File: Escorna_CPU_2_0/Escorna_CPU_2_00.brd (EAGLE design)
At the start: 50.2 x 85 mm, 59 parts, among them IC1 ULN2803, U2 ESP01, X1 AK550/2

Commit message: Act. bottom layer
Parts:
- Z1: value F/CM12P -> CFG12
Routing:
- net RAW: track 141.1 -> 181.6 mm
- net D10: track 33.0 -> 30.6 mm
- net S3: track 31.4 -> 30.8 mm
- net TX: track 22.6 -> 22.0 mm
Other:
- board text added: "1538"

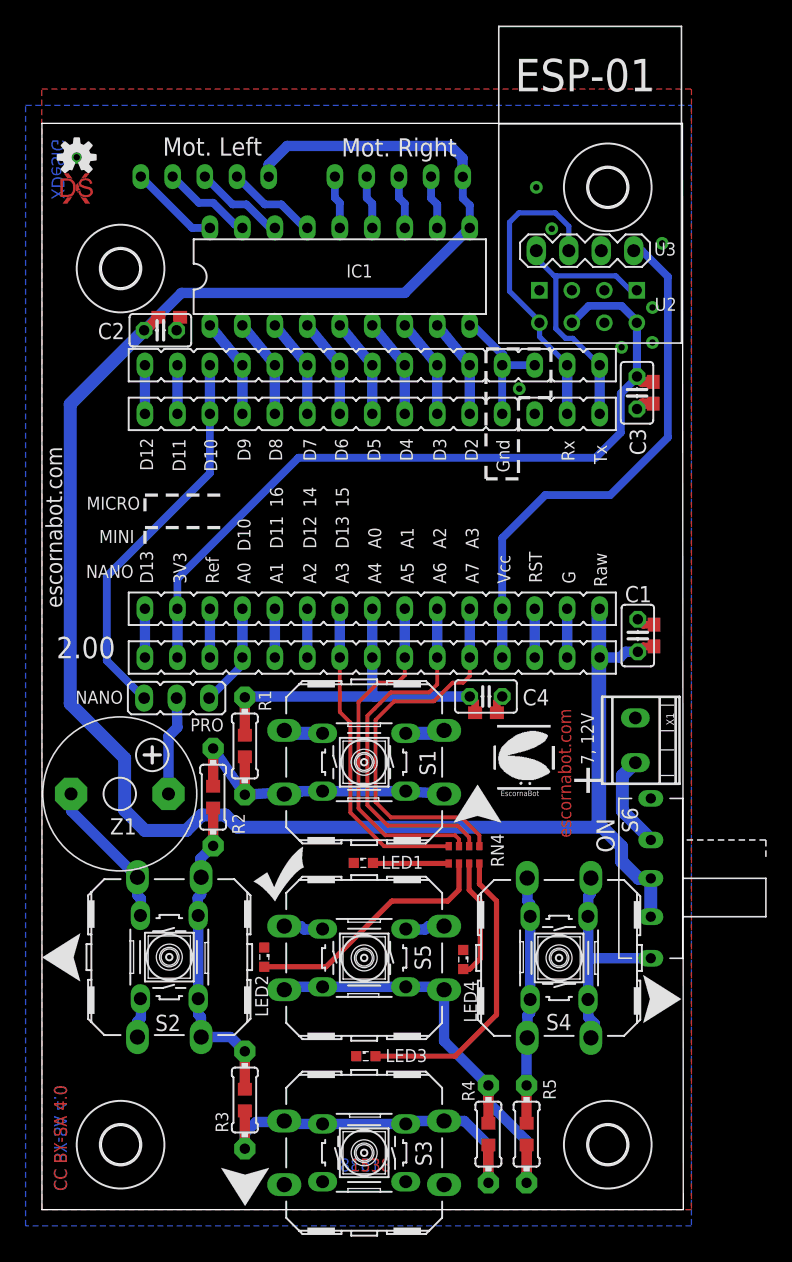
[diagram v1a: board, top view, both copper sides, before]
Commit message: Act. slikscreen
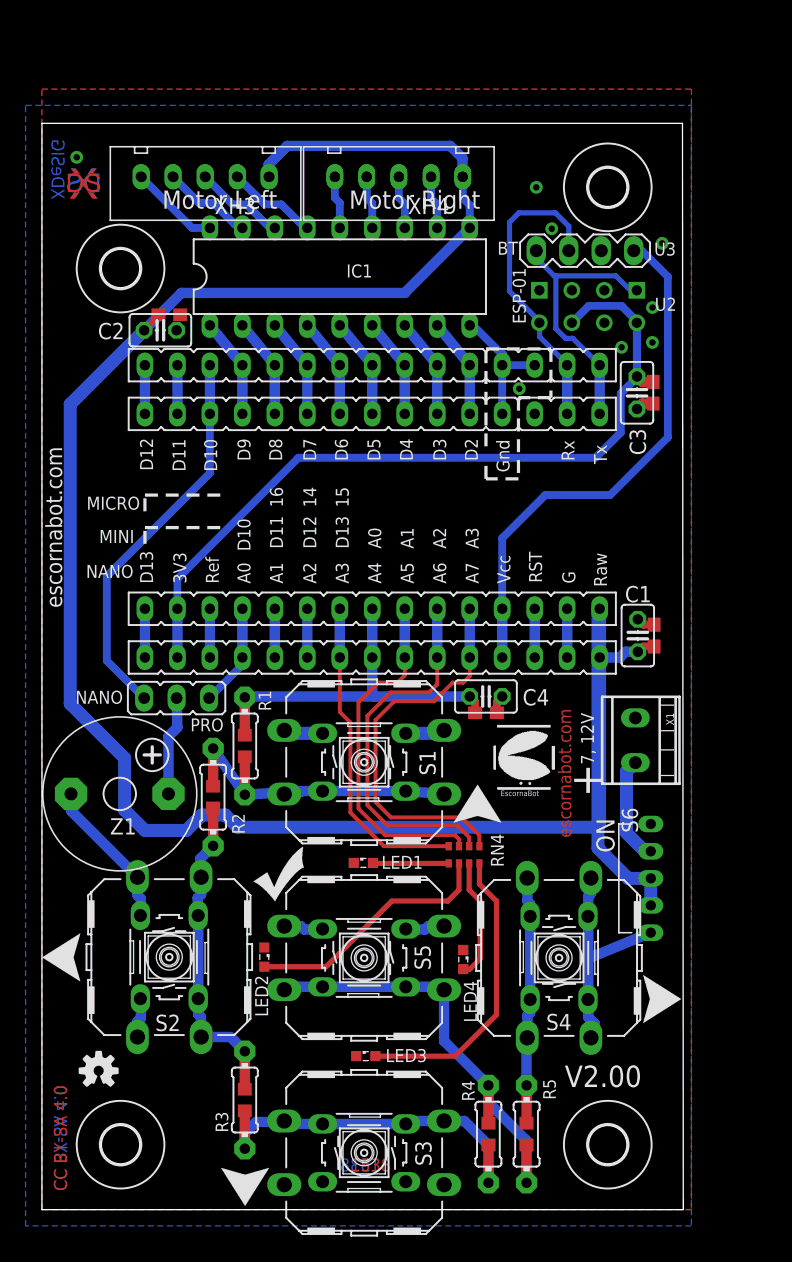
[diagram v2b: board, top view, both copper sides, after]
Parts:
- added XDS1: XDESIG, xdesig:XDESIG_CU_2
- added XH3, XH4: (no value), con-jst:B5B-XH-A
- S6: device escorna:SK-12F14-G -> escorna:SK-12D07
- moved LOGO1 71.5 mm to (4.45, 10.9)
- moved XDS 0.69 mm to (2.03, 79.1)
- moved C2.1 0.19 mm to (9.97, 70.0)
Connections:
- net ML1: now also XH3.P$5
- net ML2: now also XH3.P$4
- net ML3: now also XH3.P$3
- net ML4: now also XH3.P$2
- net MR1: now also XH4.P$5
- net MR2: now also XH4.P$4
- net MR3: now also XH4.P$3
- net MR4: now also XH4.P$2
- net RAW: now also XH3.P$1, XH4.P$1
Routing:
- net N$3: track 7.43 -> 8.28 mm
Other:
- board text added: "BT"
- board text added: "ESP-01"
- board text added: "Motor Left"
- board text added: "Motor Right"
- board text added: "V2.00"
- board text removed: "2.00"
- board text removed: "Mot. Left"
- board text removed: "Mot. Right"
